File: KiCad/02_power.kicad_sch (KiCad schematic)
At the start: 39 parts, among them J201 Barrel_Jack_Switch_Pin3Ring, U201 AMS1117-3.3, U202 TLV62569DBV

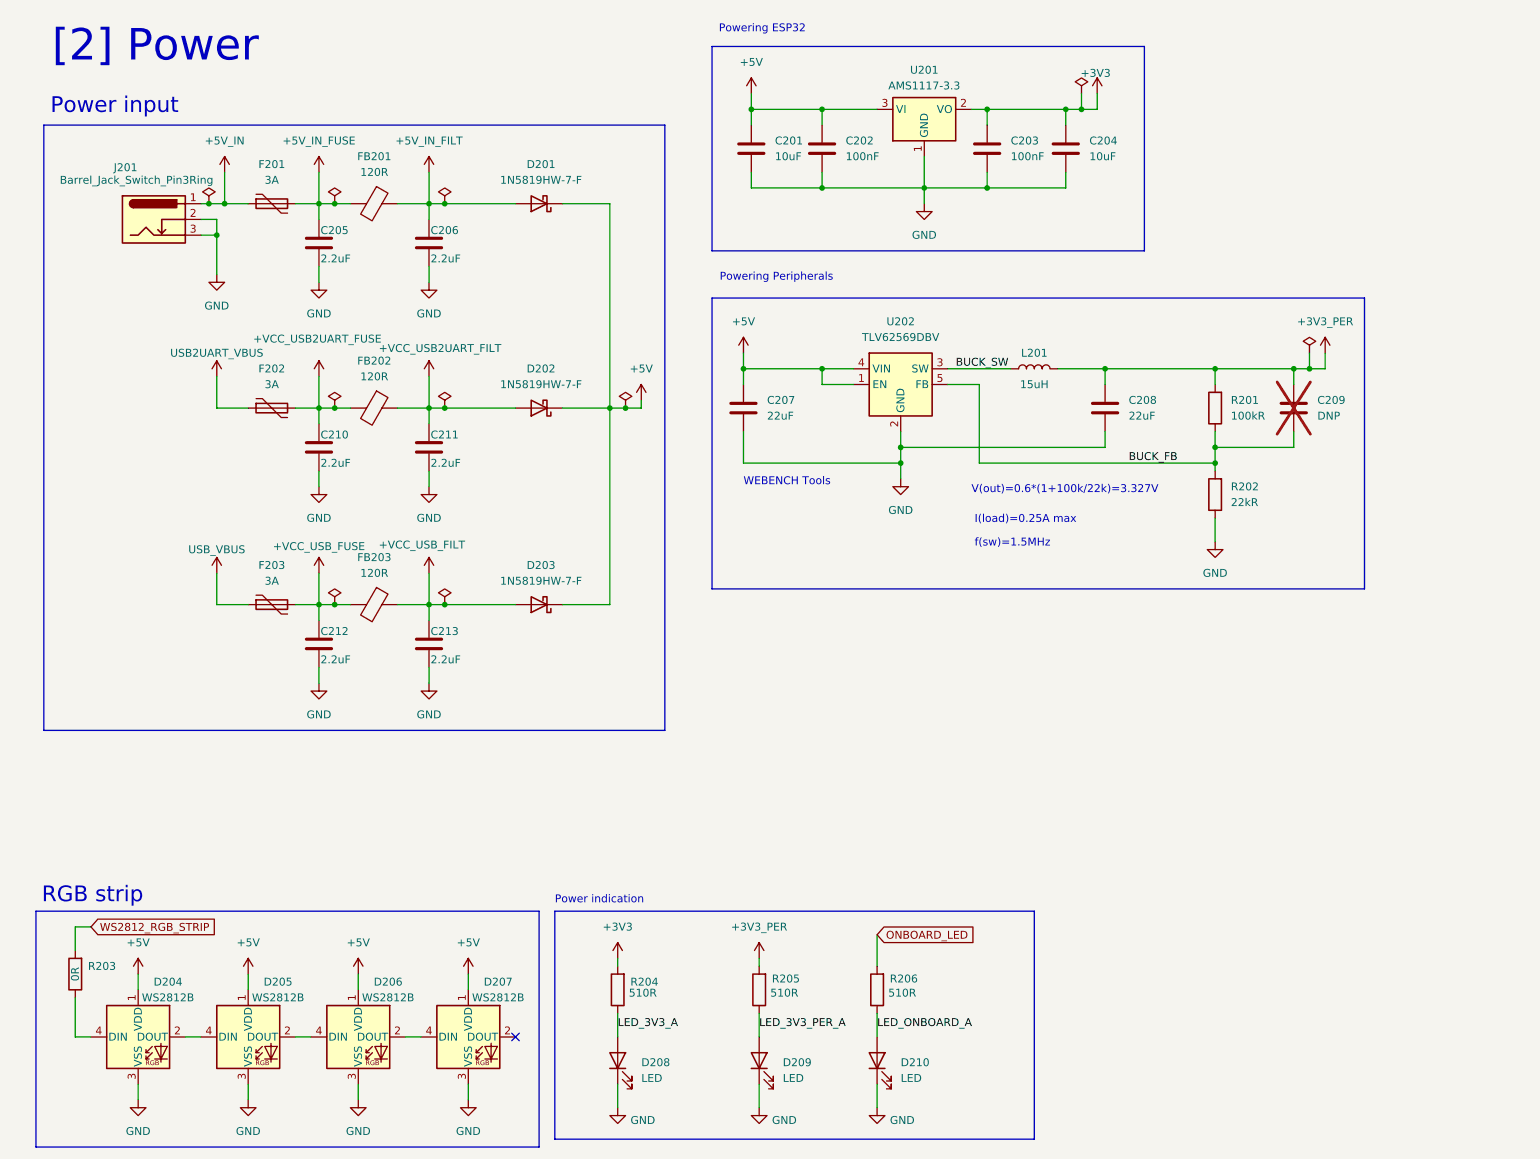
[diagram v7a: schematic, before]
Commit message: Add battery connector and charger
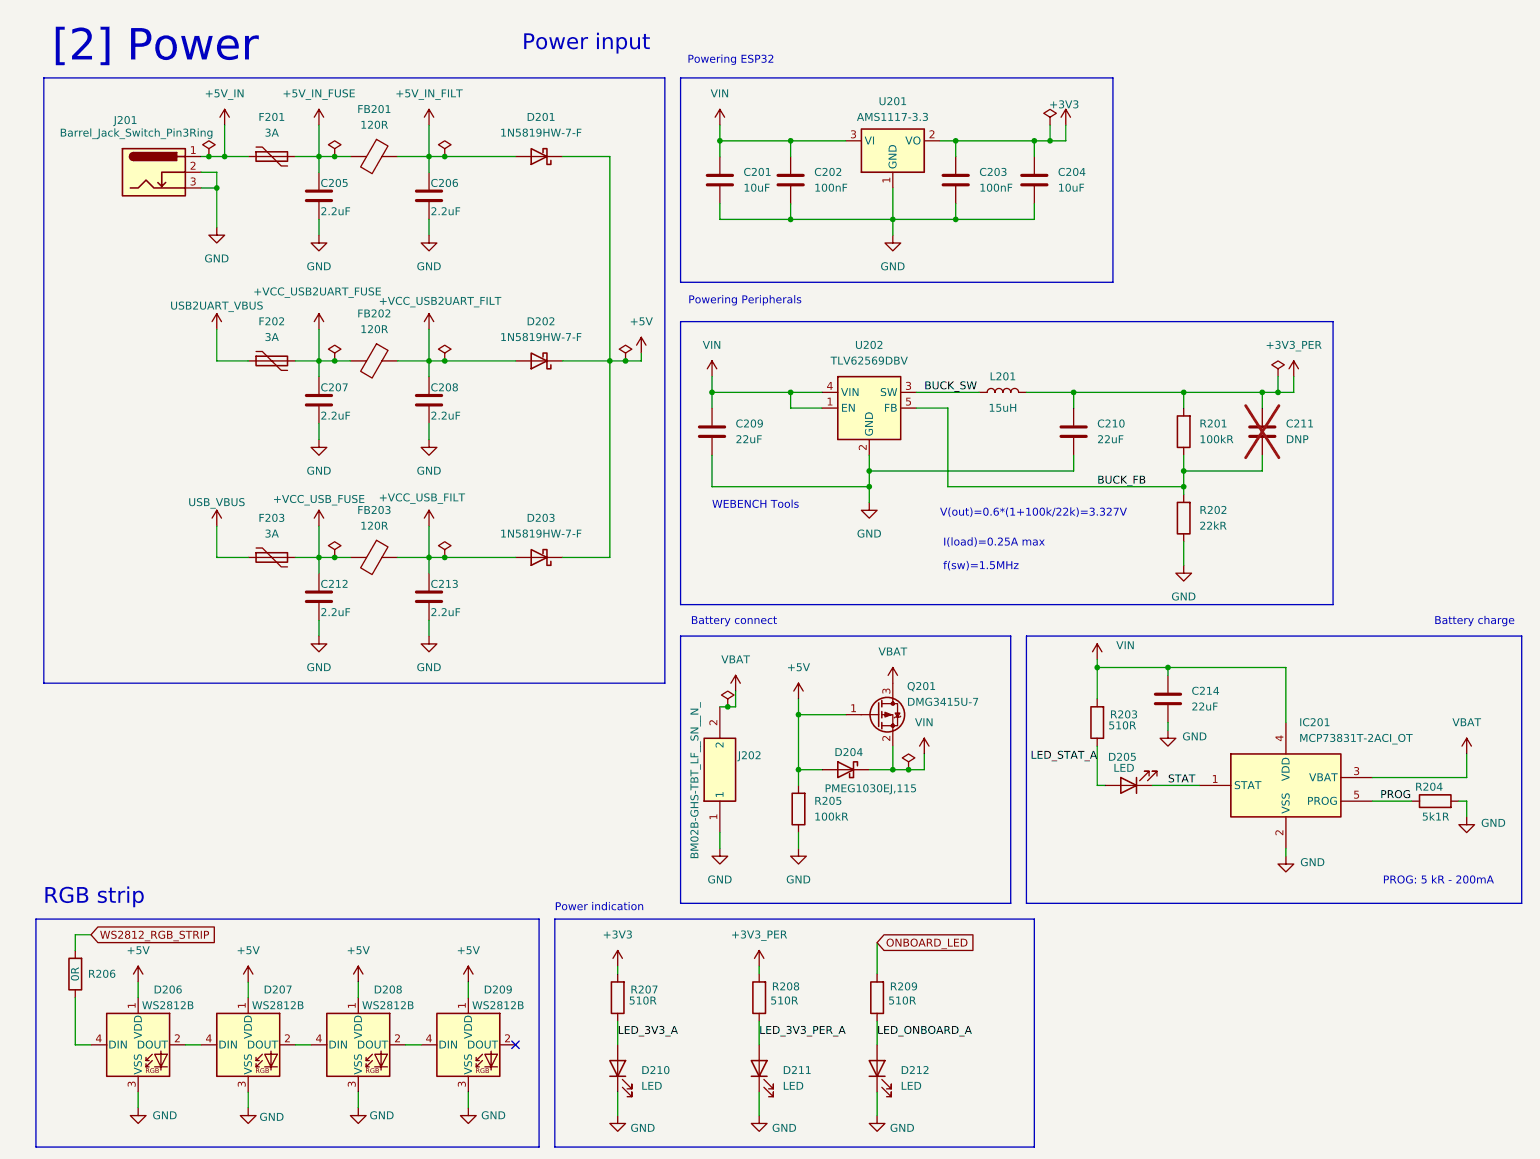
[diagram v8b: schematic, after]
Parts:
- added C214: 22uF, Capacitor_SMD:C_0603_1608Metric, symbol Device:C
- added D204: PMEG1030EJ,115, Diode_SMD:D_SOD-323F, symbol Device:D_Schottky
- added D205: LED, LED_SMD:LED_0603_1608Metric, symbol Device:LED
- added IC201: MCP73831T-2ACI_OT, esp32_s3_weather_webserver:SOT95P270X145-5N, symbol esp32_s3_weather_webserver:MCP73831T-2ACI_OT
- added J202: BM02B-GHS-TBT_LF__SN__N_, esp32_s3_weather_webserver:BM02B-GHS-TBT_1, symbol esp32_s3_weather_webserver:BM02B-GHS-TBT_LF__SN__N_
- added Q201: DMG3415U-7, Package_TO_SOT_SMD:SOT-23, symbol Transistor_FET:AO3401A
- added R203: 510R, Resistor_SMD:R_0402_1005Metric, symbol Device:R
- added R204: 5k1R, Resistor_SMD:R_0402_1005Metric, symbol Device:R
- added R205: 100kR, Resistor_SMD:R_0402_1005Metric, symbol Device:R
- renumbered C210 to C207, C211 to C208, C207 to C209, C208 to C210, C209 to C211, D204 to D206, D205 to D207, D206 to D208, D207 to D209, D208 to D210, D209 to D211, D210 to D212, R203 to R206, R204 to R207, R205 to R208, R206 to R209
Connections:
- net +5V: now also D204.2 (A), Q201.1 (G), R205.2; no longer C201.1, C202.1, C209.1, U201.3 (VI), U202.1 (EN), U202.4 (VIN)
- net GND: now also C214.2, IC201.2 (VSS), J202.1, R204.2, R205.1
- new net LED_STAT_A: D205.2 (A), R203.1
- new net PROG: IC201.5 (PROG), R204.1
- new net STAT: D205.1 (K), IC201.1 (STAT)
- new net VBAT: IC201.3 (VBAT), J202.2, Q201.3 (D)
- new net VIN: C201.1, C202.1, C209.1, C214.1, D204.1 (K), IC201.4 (VDD), Q201.2 (S), R203.2, U201.3 (VI), U202.1 (EN), U202.4 (VIN)
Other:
- note added: "Battery charge"
- note added: "Battery connect"
- note added: "PROG: 5 kR - 200mA"
- moved on the sheet: C201, C202, C203, C204, C205, C206, C207, C208, C209, C210, C211, C212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
